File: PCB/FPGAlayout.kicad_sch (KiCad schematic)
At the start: 6 parts, among them U3 XC7A100T-FTG256

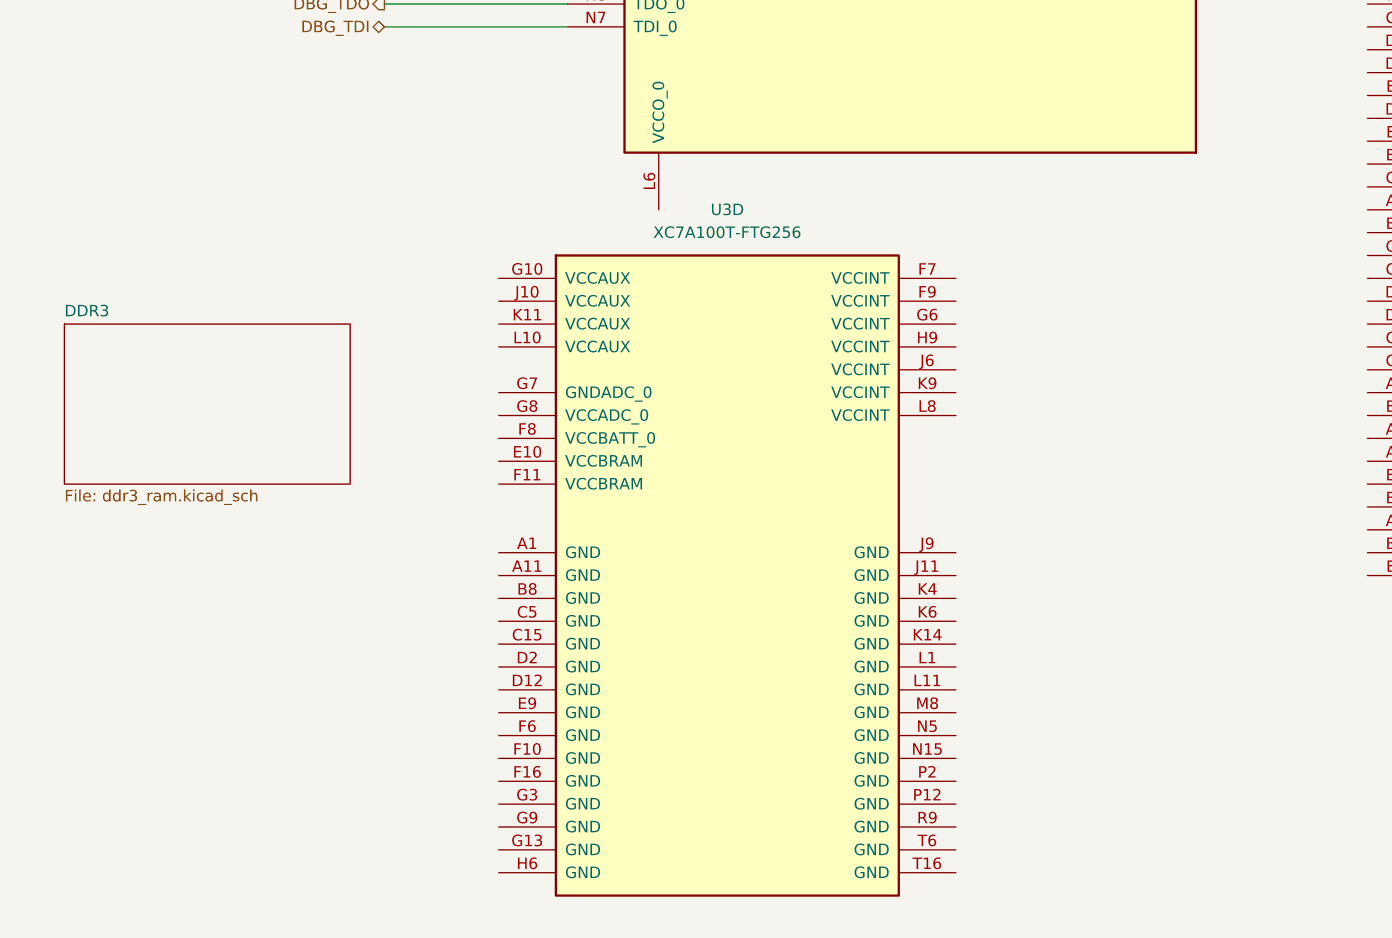
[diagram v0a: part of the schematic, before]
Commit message: Finish MCU Master to Slave Traces for QSPI and Reorganize RootSheet
Signed-off-by: Daniel Yang Hansen <daniel.yang.hansen@gmail.com>
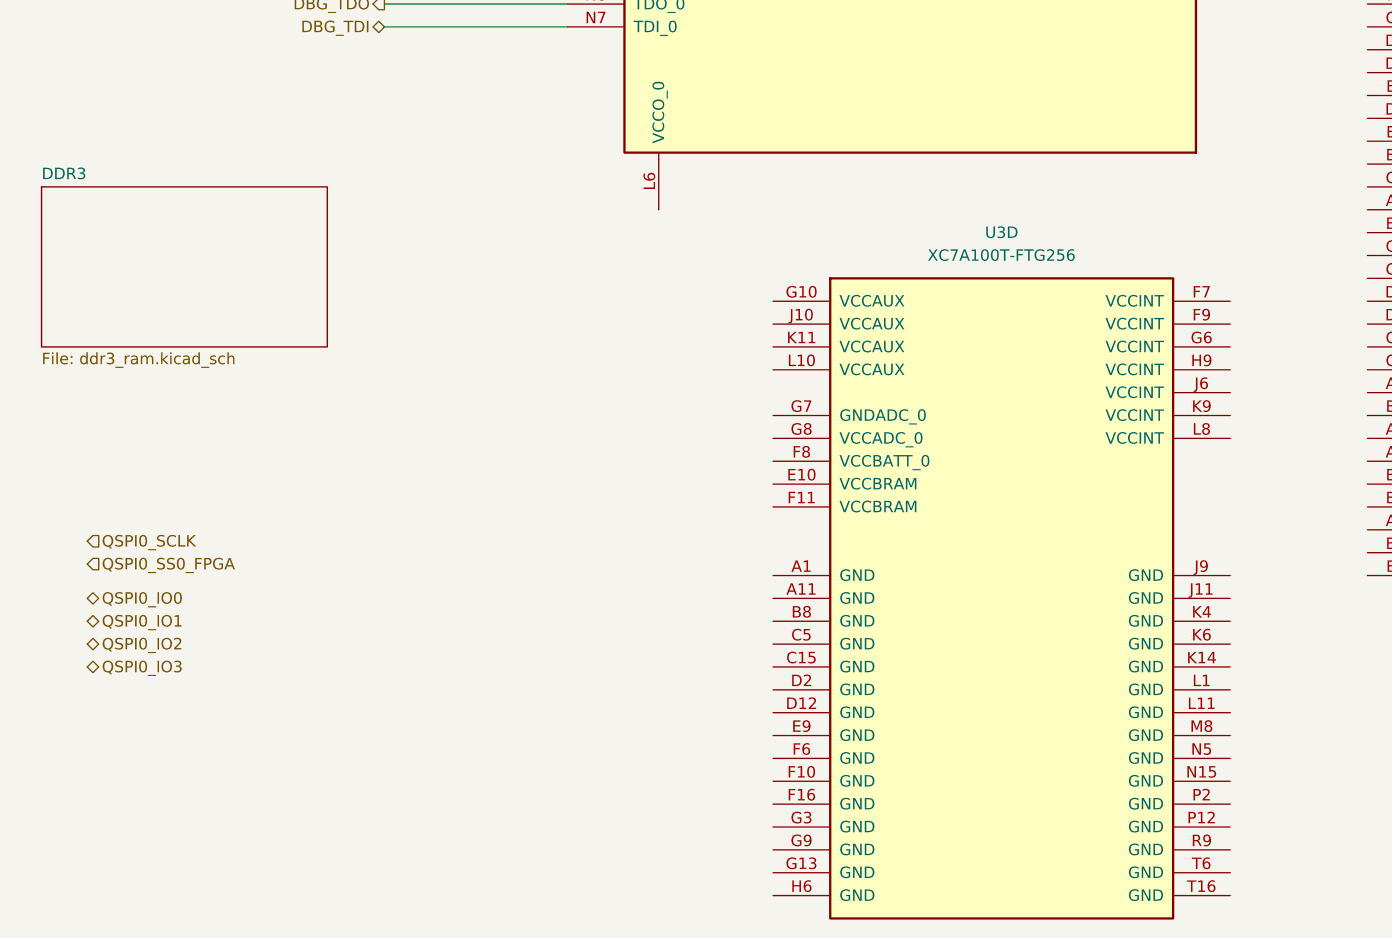
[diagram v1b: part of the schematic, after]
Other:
- moved on the sheet: U3D
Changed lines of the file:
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@@
     (stroke (width 0) (type default))
+  )
+  (hierarchical_label "QSPI0_IO1" (shape bidirectional) (at 24.13 152.4 0) (fields_autoplaced)
+    (effects (font (size 1.27 1.27)) (justify left))
+  )
+  (hierarchical_label "QSPI0_SS0_FPGA" (shape input) (at 24.13 146.05 0) (fields_autoplaced)
+    (effects (font (size 1.27 1.27)) (justify left))
   )
   (hierarchical_label "PROGRAM_B_0" (shape output) (at 62.23 55.88 180) (fields_autoplaced)
@@
     (effects (font (size 1.27 1.27)) (justify right))
   )
+  (hierarchical_label "QSPI0_SCLK" (shape input) (at 24.13 143.51 0) (fields_autoplaced)
+    (effects (font (size 1.27 1.27)) (justify left))
+  )
+  (hierarchical_label "QSPI0_IO2" (shape bidirectional) (at 24.13 154.94 0) (fields_autoplaced)
+    (effects (font (size 1.27 1.27)) (justify left))
+  )
   (hierarchical_label "DBG_TMS" (shape input) (at 57.15 81.28 180) (fields_autoplaced)
     (effects (font (size 1.27 1.27)) (justify right))
   )
+  (hierarchical_label "QSPI0_IO0" (shape bidirectional) (at 24.13 149.86 0) (fields_autoplaced)
+    (effects (font (size 1.27 1.27)) (justify left))
+  )
   (hierarchical_label "DBG_TCK" (shape input) (at 57.15 78.74 180) (fields_autoplaced)
     (effects (font (size 1.27 1.27)) (justify right))
@@
   (hierarchical_label "DBG_TDI" (shape bidirectional) (at 57.15 86.36 180) (fields_autoplaced)
     (effects (font (size 1.27 1.27)) (justify right))
+  )
+  (hierarchical_label "QSPI0_IO3" (shape bidirectional) (at 24.13 157.48 0) (fields_autoplaced)
+    (effects (font (size 1.27 1.27)) (justify left))
   )
   (hierarchical_label "DBG_TDO" (shape output) (at 57.15 83.82 180) (fields_autoplaced)
@@
     )
   )
-  (symbol (lib_id "FPGA_Xilinx_Artix7:XC7A100T-FTG256") (at 95.25 147.32 0) (unit 4)
+  (symbol (lib_id "FPGA_Xilinx_Artix7:XC7A100T-FTG256") (at 125.73 149.86 0) (unit 4)
     (in_bom yes) (on_board yes) (dnp no) (fields_autoplaced)
-    (property "Reference" "U3" (at 95.25 106.68 0)
+    (property "Reference" "U3" (at 125.73 109.22 0)
       (effects (font (size 1.27 1.27)))
     )
-    (property "Value" "XC7A100T-FTG256" (at 95.25 109.22 0)
+    (property "Value" "XC7A100T-FTG256" (at 125.73 111.76 0)
       (effects (font (size 1.27 1.27)))
     )
-    (property "Footprint" "" (at 95.25 147.32 0)
-      (effects (font (size 1.27 1.27)) hide)
-    )
-    (property "Datasheet" "" (at 95.25 147.32 0)
+    (property "Footprint" "" (at 125.73 149.86 0)
+      (effects (font (size 1.27 1.27)) hide)
+    )
+    (property "Datasheet" "" (at 125.73 149.86 0)
       (effects (font (size 1.27 1.27)))
     )
@@
     )
   )
-  (sheet (at 21.59 119.38) (size 31.75 17.78) (fields_autoplaced)
+  (sheet (at 19.05 104.14) (size 31.75 17.78) (fields_autoplaced)
     (stroke (width 0.1524) (type solid))
     (fill (color 0 0 0 0.0000))
-    (property "Sheetname" "DDR3" (at 21.59 118.6684 0)
+    (property "Sheetname" "DDR3" (at 19.05 103.4284 0)
       (effects (font (size 1.27 1.27)) (justify left bottom))
     )
-    (property "Sheetfile" "ddr3_ram.kicad_sch" (at 21.59 137.7446 0)
+    (property "Sheetfile" "ddr3_ram.kicad_sch" (at 19.05 122.5046 0)
       (effects (font (size 1.27 1.27)) (justify left top))
     )

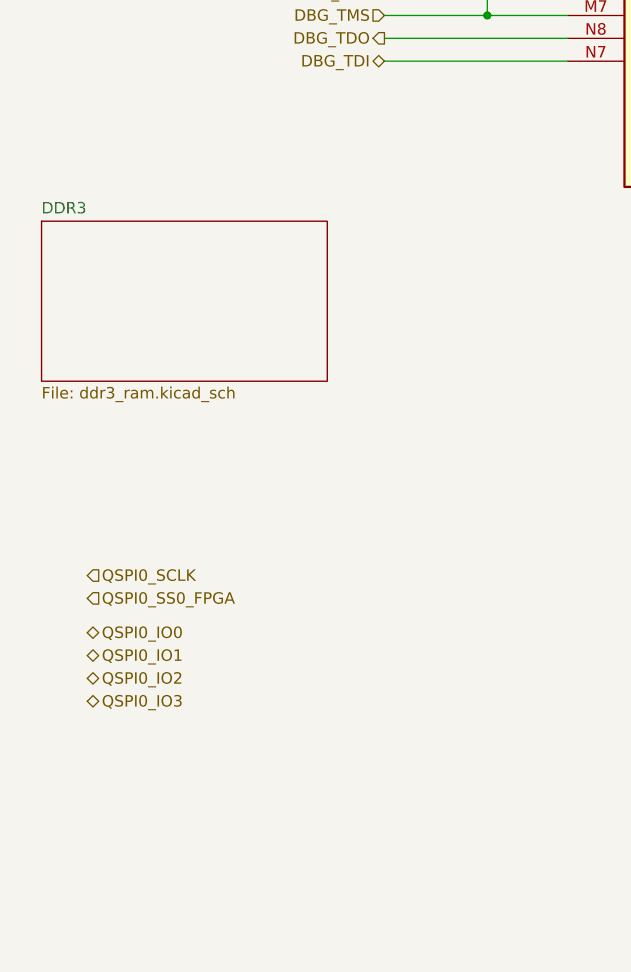
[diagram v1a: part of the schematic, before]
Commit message: Slight restructuring of FPGA SRAM Naming
Signed-off-by: Daniel Yang Hansen <daniel.yang.hansen@gmail.com>
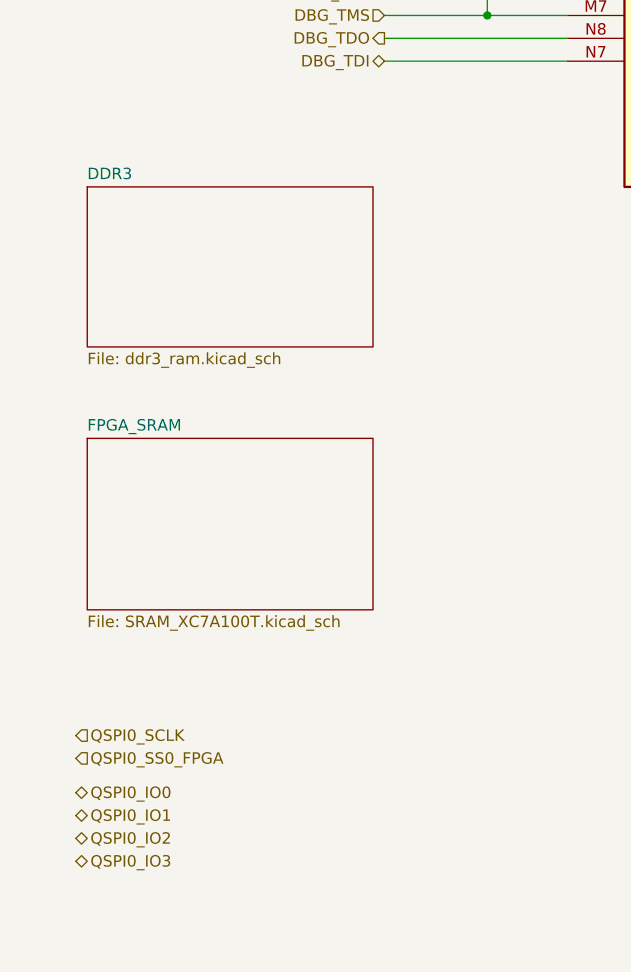
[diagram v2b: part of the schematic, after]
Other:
- added sheet FPGA_SRAM (SRAM_XC7A100T.kicad_sch)
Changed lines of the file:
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@@
     (stroke (width 0) (type default))
   )
-  (hierarchical_label "QSPI0_IO1" (shape bidirectional) (at 24.13 152.4 0) (fields_autoplaced)
+  (hierarchical_label "QSPI0_IO1" (shape bidirectional) (at 22.86 170.18 0) (fields_autoplaced)
     (effects (font (size 1.27 1.27)) (justify left))
   )
-  (hierarchical_label "QSPI0_SS0_FPGA" (shape input) (at 24.13 146.05 0) (fields_autoplaced)
+  (hierarchical_label "QSPI0_SS0_FPGA" (shape input) (at 22.86 163.83 0) (fields_autoplaced)
     (effects (font (size 1.27 1.27)) (justify left))
   )
@@
     (effects (font (size 1.27 1.27)) (justify right))
   )
-  (hierarchical_label "QSPI0_SCLK" (shape input) (at 24.13 143.51 0) (fields_autoplaced)
+  (hierarchical_label "QSPI0_SCLK" (shape input) (at 22.86 161.29 0) (fields_autoplaced)
     (effects (font (size 1.27 1.27)) (justify left))
   )
-  (hierarchical_label "QSPI0_IO2" (shape bidirectional) (at 24.13 154.94 0) (fields_autoplaced)
+  (hierarchical_label "QSPI0_IO2" (shape bidirectional) (at 22.86 172.72 0) (fields_autoplaced)
     (effects (font (size 1.27 1.27)) (justify left))
   )
@@
     (effects (font (size 1.27 1.27)) (justify right))
   )
-  (hierarchical_label "QSPI0_IO0" (shape bidirectional) (at 24.13 149.86 0) (fields_autoplaced)
+  (hierarchical_label "QSPI0_IO0" (shape bidirectional) (at 22.86 167.64 0) (fields_autoplaced)
     (effects (font (size 1.27 1.27)) (justify left))
   )
@@
     (effects (font (size 1.27 1.27)) (justify right))
   )
-  (hierarchical_label "QSPI0_IO3" (shape bidirectional) (at 24.13 157.48 0) (fields_autoplaced)
+  (hierarchical_label "QSPI0_IO3" (shape bidirectional) (at 22.86 175.26 0) (fields_autoplaced)
     (effects (font (size 1.27 1.27)) (justify left))
   )
@@
     )
   )
-  (sheet (at 19.05 104.14) (size 31.75 17.78) (fields_autoplaced)
+  (sheet (at 24.13 128.27) (size 31.75 19.05) (fields_autoplaced)
     (stroke (width 0.1524) (type solid))
     (fill (color 0 0 0 0.0000))
-    (property "Sheetname" "DDR3" (at 19.05 103.4284 0)
+    (property "Sheetname" "FPGA_SRAM" (at 24.13 127.5584 0)
       (effects (font (size 1.27 1.27)) (justify left bottom))
     )
-    (property "Sheetfile" "ddr3_ram.kicad_sch" (at 19.05 122.5046 0)
+    (property "Sheetfile" "SRAM_XC7A100T.kicad_sch" (at 24.13 147.9046 0)
       (effects (font (size 1.27 1.27)) (justify left top))
     )
+    (instances
+      (project "RayTracingPCB"
+        (path "/e9047d94-28be-4266-894b-6ee25ef088bd/5a7a2c0a-f09d-4b4f-9411-f51dd121457c" (page "10"))
+      )
+    )
+  )
+  (sheet (at 24.13 100.33) (size 31.75 17.78) (fields_autoplaced)
+    (stroke (width 0.1524) (type solid))
+    (fill (color 0 0 0 0.0000))
+    (property "Sheetname" "DDR3" (at 24.13 99.6184 0)
+      (effects (font (size 1.27 1.27)) (justify left bottom))
+    )
+    (property "Sheetfile" "ddr3_ram.kicad_sch" (at 24.13 118.6946 0)
+      (effects (font (size 1.27 1.27)) (justify left top))
+    )
